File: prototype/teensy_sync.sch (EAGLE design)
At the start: 15 parts, among them U1 MPU-6000QFN-24

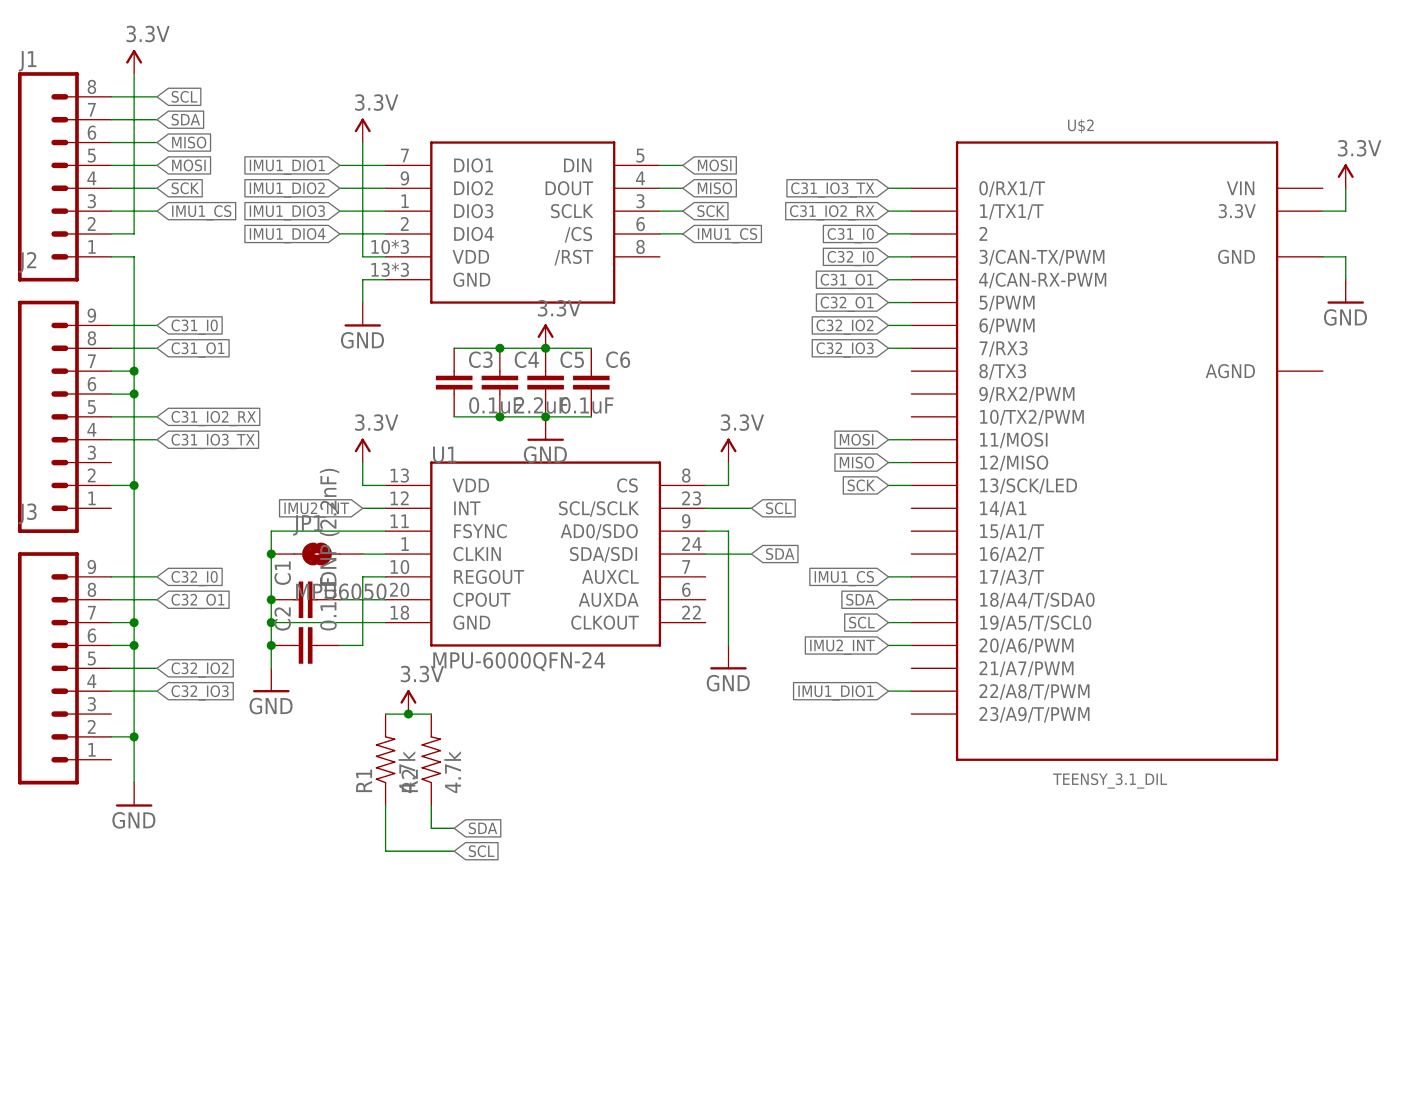
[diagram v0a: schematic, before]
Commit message: Updated brd and sch file to reflect prototype boards ordered.
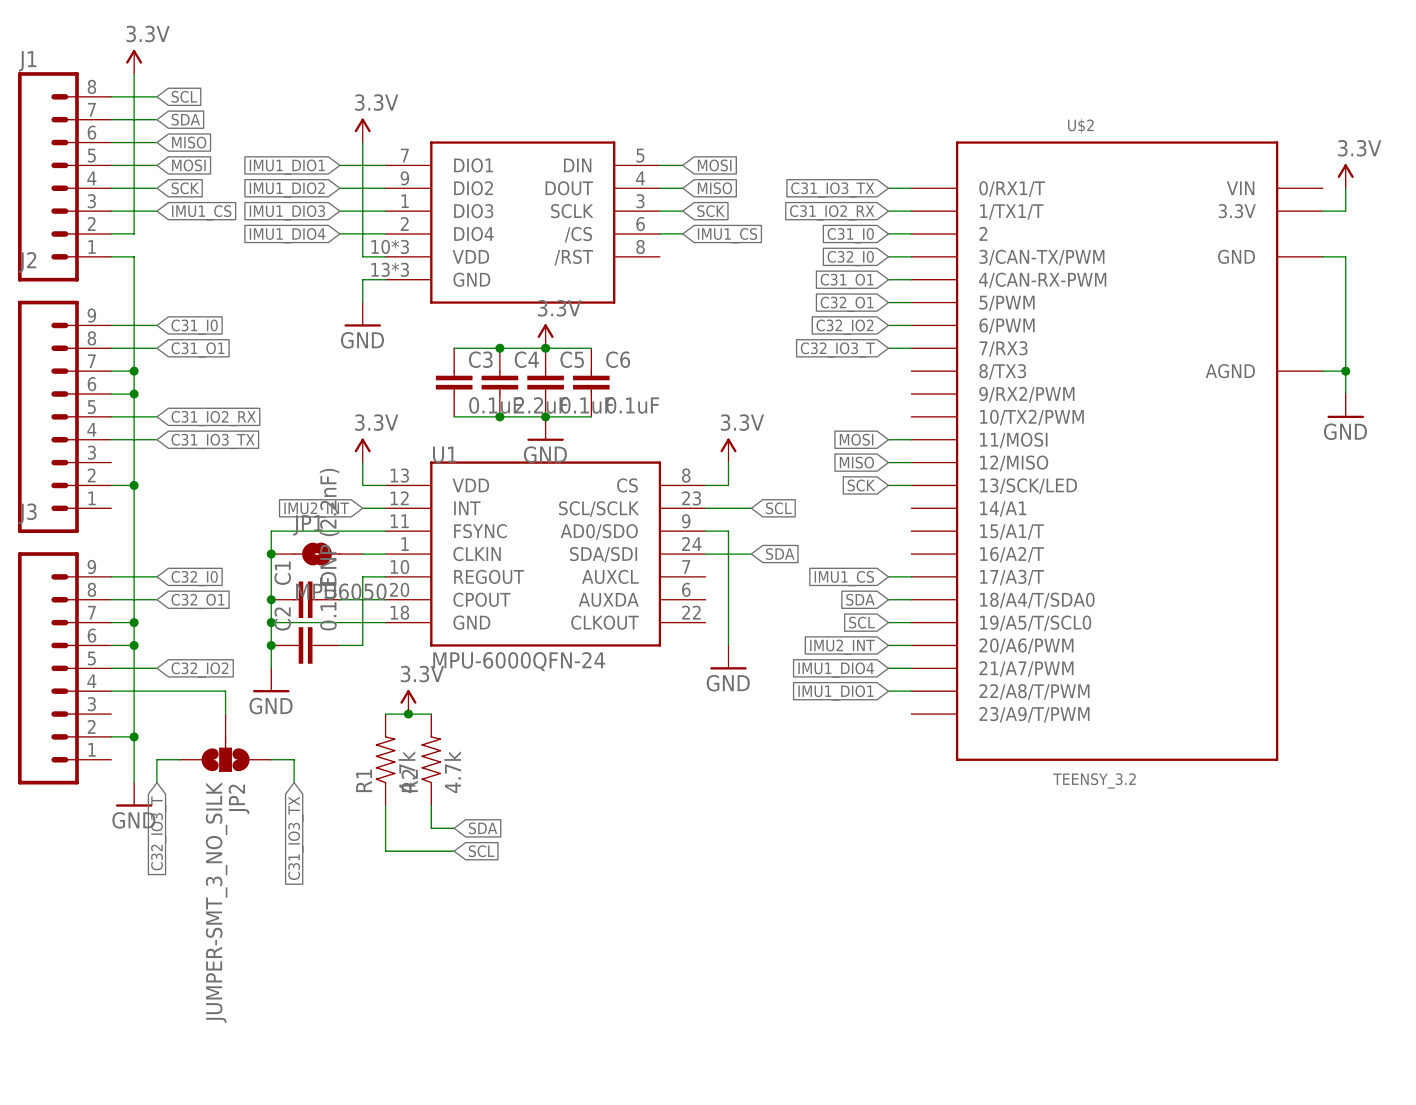
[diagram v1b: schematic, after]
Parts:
- added JP2: JUMPER-SMT_3_NO_SILK, SparkFun-Jumpers:JUMPER-SMT_3_NO_SILK
- C6: value (none) -> 0.1uF
- U$2: value TEENSY_3.1_DIL -> TEENSY_3.2
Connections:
- new net C32_IO3_T: JP2.3, U$2.7/RX3
- net C31_IO3_TX: now also JP2.1
- net C32_IO3: now also JP2.2; no longer U$2.7/RX3
- net GND: now also U$2.AGND
- net IMU1_DIO4: now also U$2.21/A7/PWM
